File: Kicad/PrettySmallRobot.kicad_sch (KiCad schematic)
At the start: 53 parts

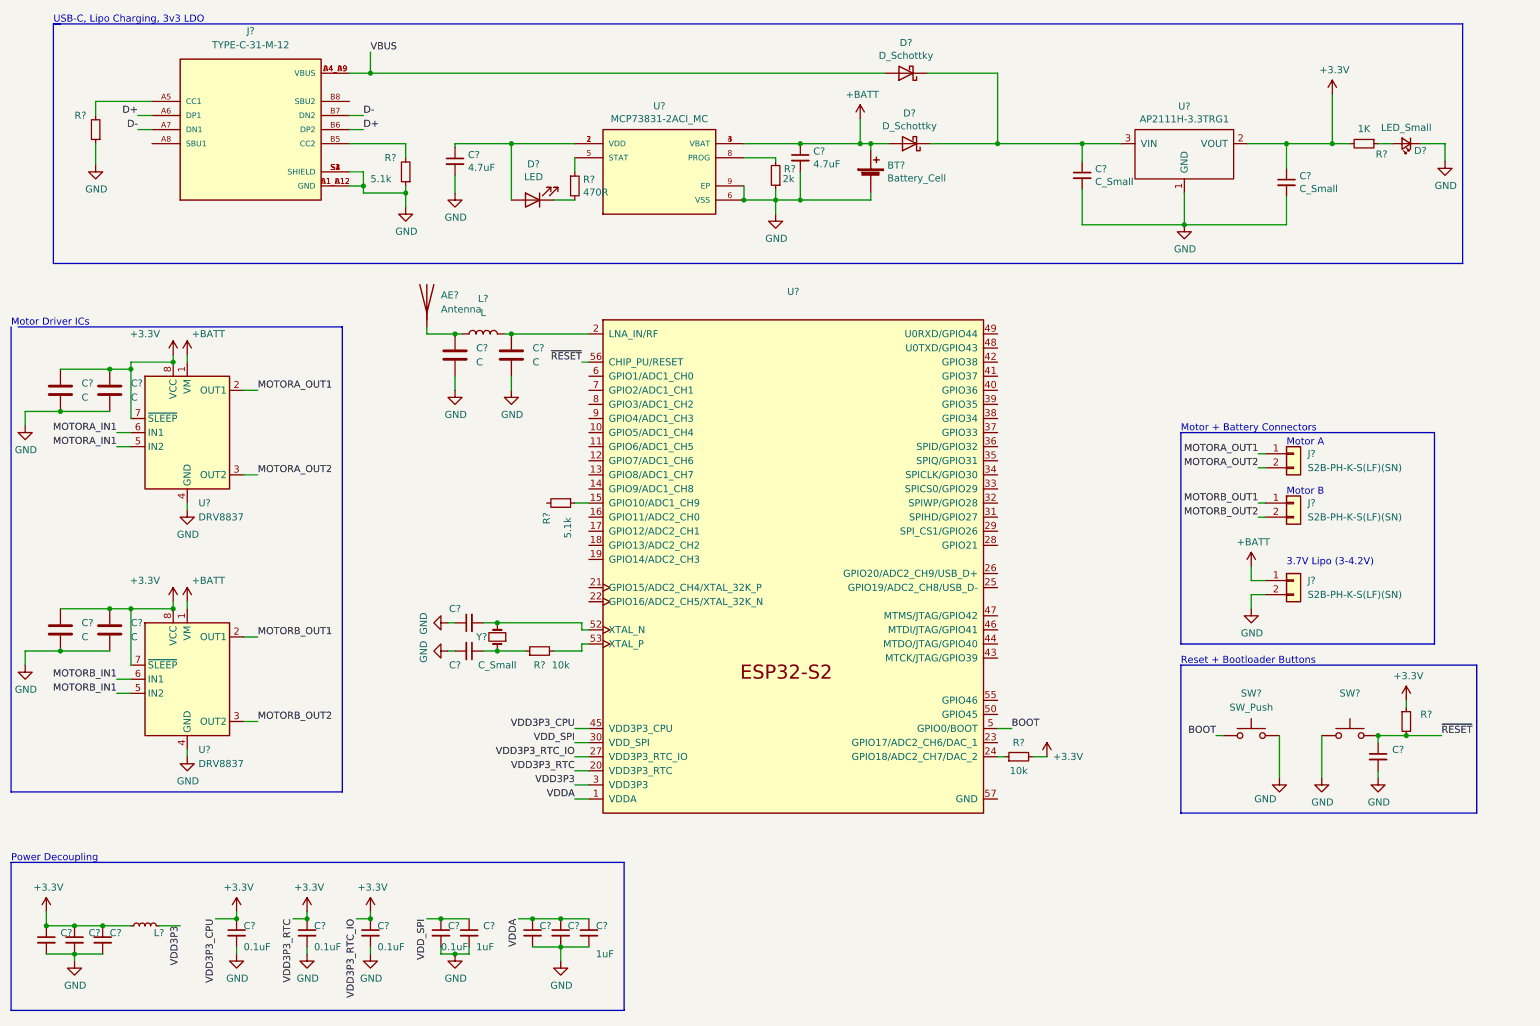
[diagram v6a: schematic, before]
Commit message: worked on motor driver signals
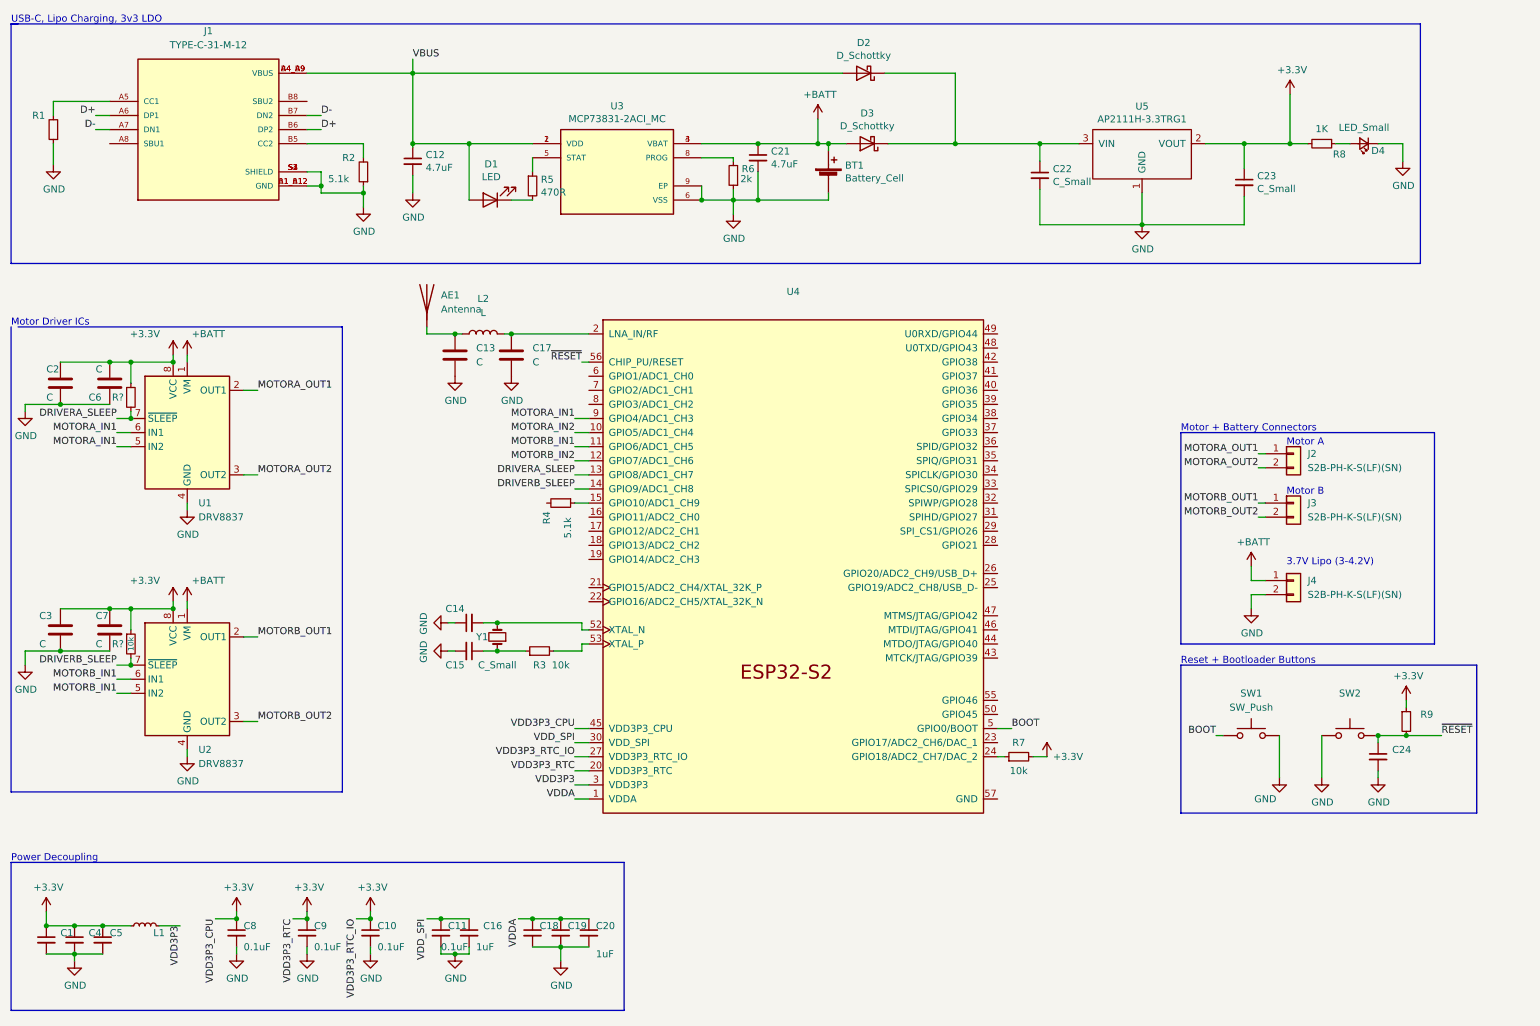
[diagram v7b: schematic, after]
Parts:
- added R?: (no value), symbol Device:R_Small
- added R?: 10k, symbol Device:R_Small
- gave numbers to parts that had none: 53
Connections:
- net +3V3: now also R?.1, R?.1; no longer U1.7 (~{SLEEP}), U2.7 (~{SLEEP})
- net MOTORA_IN1: now also U4.9 (GPIO4/ADC1_CH3)
- net MOTORB_IN1: now also U4.11 (GPIO6/ADC1_CH5)
- net VBUS: now also C12.1, D1.2 (A), U3.1 (VDD), U3.2 (VDD)
- net MOTORA_IN2: now reaches U4.10 (GPIO5/ADC1_CH4)
- net MOTORB_IN2: now reaches U4.12 (GPIO7/ADC1_CH6)
- net DRIVERA_SLEEP: now reaches U4.13 (GPIO8/ADC1_CH7)
- net DRIVERA_SLEEP: now also U1.7 (~{SLEEP}), R?.2
- net DRIVERB_SLEEP: now reaches U4.14 (GPIO9/ADC1_CH8)
- net DRIVERB_SLEEP: now also U2.7 (~{SLEEP}), R?.2
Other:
- moved on the sheet: BT1, C12, C2, C21, C22, C23, C6, D1, D2, D3, D4, J1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

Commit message: added testpoint on 3v3
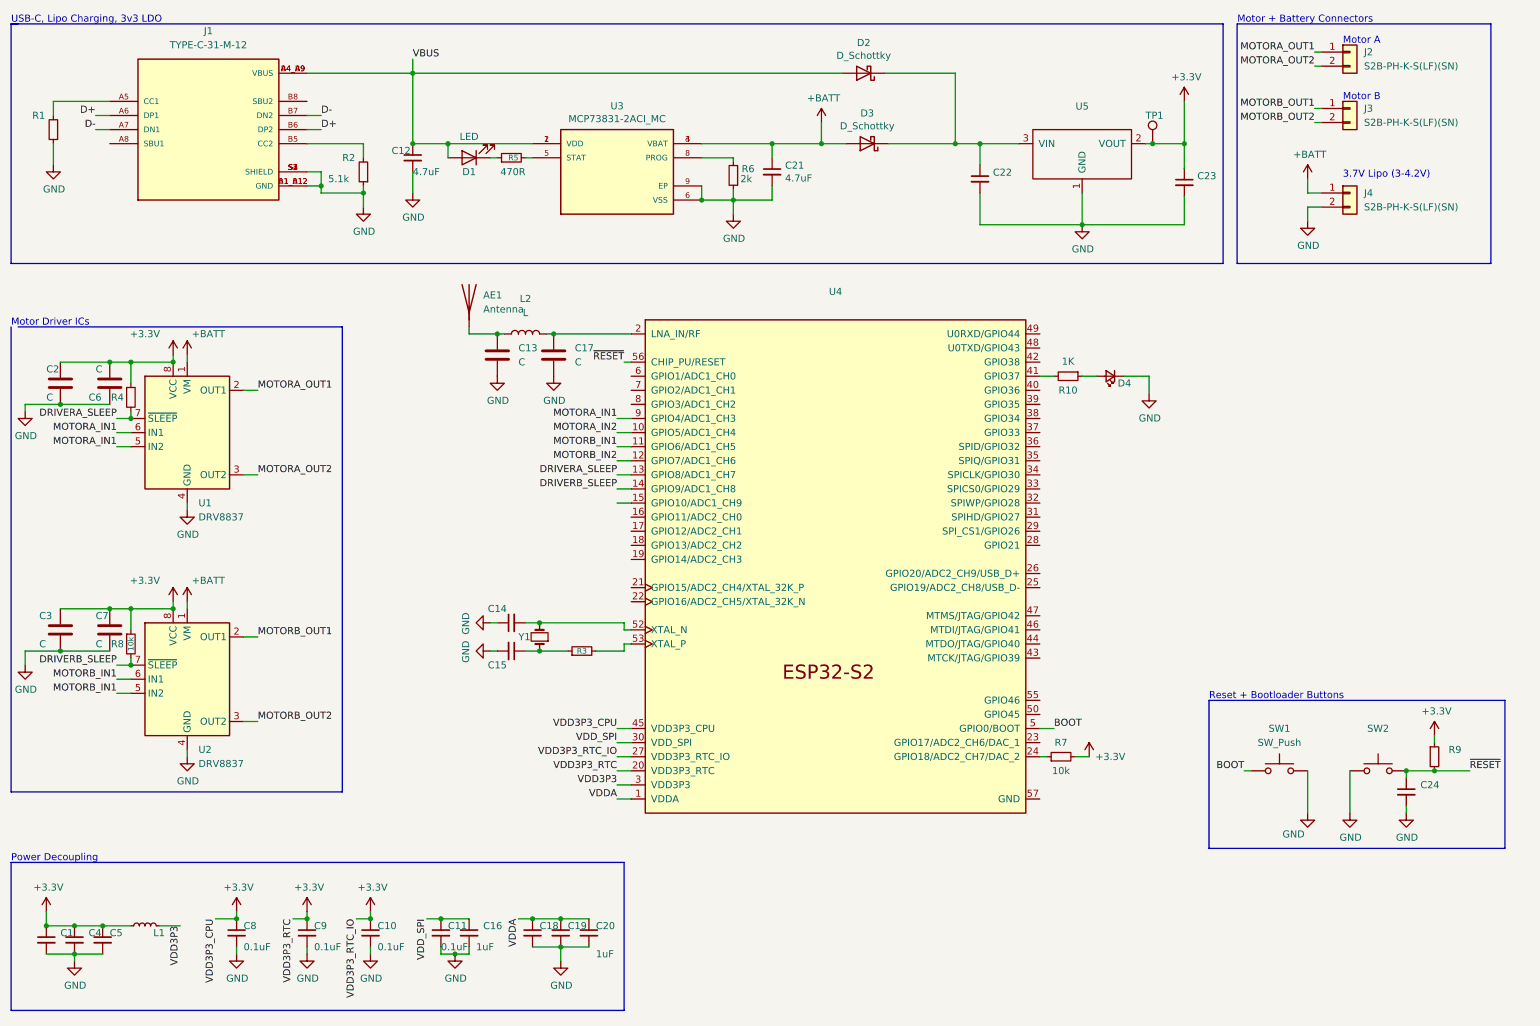
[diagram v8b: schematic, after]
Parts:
- removed BT1: Battery_Cell, symbol Device:Battery_Cell
- removed R4: 5.1k, symbol Device:R_Small
- removed R8: 1K, symbol Device:R_Small
- added R10: 1K, symbol Device:R_Small
- added TP1: (no value), symbol Connector:TestPoint
- C14: LCSC (none) -> C1547
- C15: value C_Small -> (none); LCSC (none) -> C1547
- C22, C23: value C_Small -> (none)
- D4: value LED_Small -> (none)
- R3: value 10k -> (none)
- U3: footprint SON50P200X300X100-9N -> (none)
- U5: value AP2111H-3.3TRG1 -> (none); LCSC (none) -> C155300
- Y1: LCSC (none) -> C252255
- gave numbers to parts that had none: 2
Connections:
- net +3V3: now also TP1.1
- net at D4.2 (A): now also R10.1
- net at U3.5 (STAT): now also R5.2; no longer R5.1
- net at D1.1 (K): now also R5.1; no longer R5.2
- net at U4.41 (GPIO37): now also R10.2
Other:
- moved on the sheet: AE1, C12, C13, C14, C15, C17, C21, C22, C23, C24, D1, J2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
